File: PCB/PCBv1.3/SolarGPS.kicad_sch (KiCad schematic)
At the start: 54 parts, among them J1 Conn_01x24_Female, J2 Solar1+, J3 GND, J4 Conn_02x03_Odd_Even, J5 Solar2+, J6 GND, J7 Screw_Terminal_01x01, J8 Conn_01x04_Male, Q1 Q_NMOS_GSD, U1 STM32L011G4Ux, U2 MAX-M10Q, U6 LIS3DH, U7 TPS63802, Y1 32.768

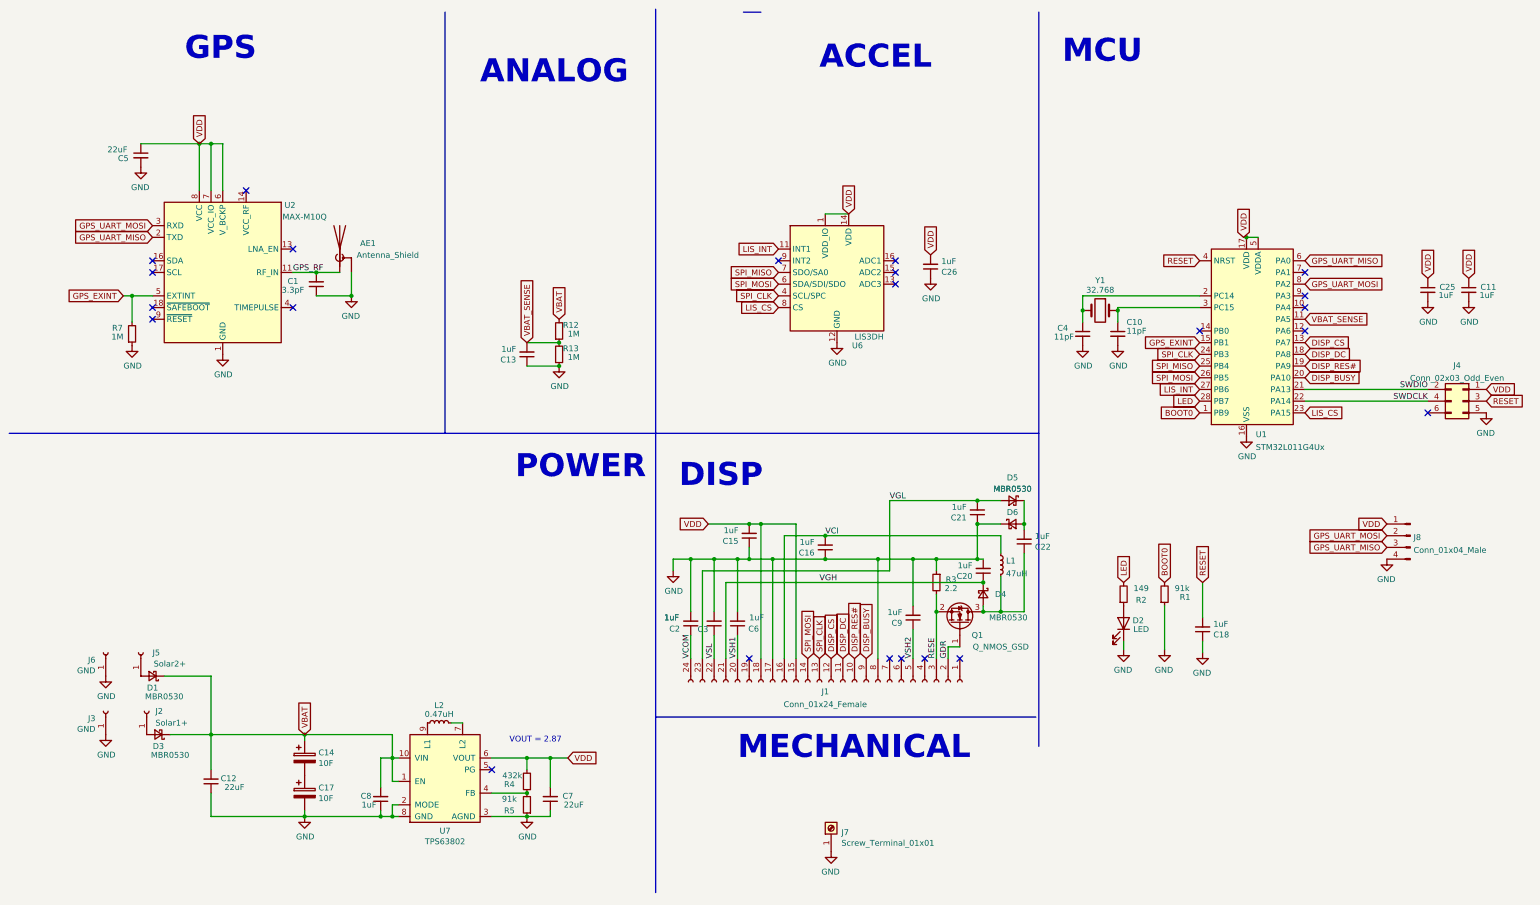
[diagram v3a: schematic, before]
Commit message: Rework power system for hybrid cap and bq25770
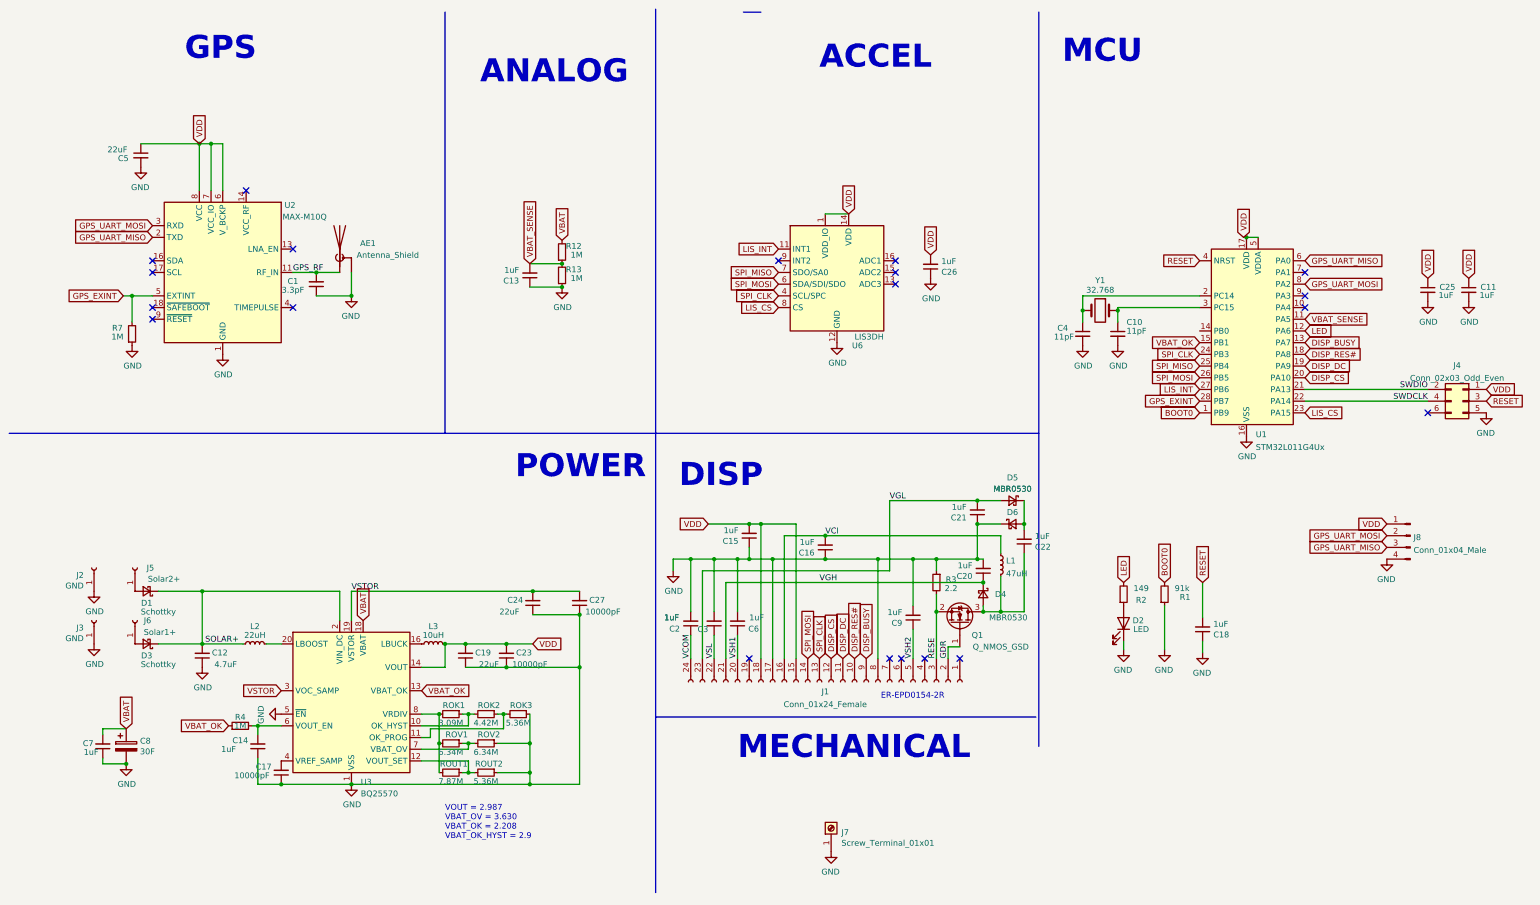
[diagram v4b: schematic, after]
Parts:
- removed C14, C17: 10F, Heliograph:SCCT20E106SRB_SMD, symbol Device:CP
- removed C8: 1uF, Capacitor_SMD:C_0603_1608Metric, symbol Device:C_Small
- removed R5: 91k, Resistor_SMD:R_0603_1608Metric, symbol Device:R_Small
- removed U7: TPS63802, Heliograph:VREG_TPS63802DLAR, symbol Heliograph:TPS63802-VeridianDesigns
- added C14: 1uF, Capacitor_SMD:C_0603_1608Metric, symbol Device:C_Small
- added C17, C23, C27: 10000pF, Capacitor_SMD:C_0603_1608Metric, symbol Device:C_Small
- added C19, C24: 22uF, Capacitor_SMD:C_0805_2012Metric, symbol Device:C_Small
- added C8: 30F, Heliograph:SCCT30E156SRB, symbol Device:CP
- added L3: 10uH, Heliograph:744029100, symbol Device:L_Small
- added ROK1: 3.09M, Resistor_SMD:R_0603_1608Metric, symbol Device:R_Small
- added ROK2: 4.42M, Resistor_SMD:R_0603_1608Metric, symbol Device:R_Small
- added ROK3, ROUT2: 5.36M, Resistor_SMD:R_0603_1608Metric, symbol Device:R_Small
- added ROUT1: 7.87M, Resistor_SMD:R_0603_1608Metric, symbol Device:R_Small
- added ROV1, ROV2: 6.34M, Resistor_SMD:R_0603_1608Metric, symbol Device:R_Small
- added U3: BQ25570, Package_DFN_QFN:QFN-20-1EP_3.5x3.5mm_P0.5mm_EP2x2mm, symbol Battery_Management:BQ25570
- C12: value 22uF -> 4.7uF; footprint Capacitor_SMD:C_0603_1608Metric -> Capacitor_SMD:C_0805_2012Metric; Part GRM187R61A226ME15 -> (none)
- C7: value 22uF -> 1uF; Part GRM187R61A226ME15 -> (none)
- D1, D3: value MBR0530 -> Schottky; footprint Diode_SMD:D_SOD-123 -> Diode_SMD:D_SOD-323_HandSoldering
- J2: value Solar1+ -> GND
- J6: value GND -> Solar1+
- L2: value 0.47uH -> 22uH; footprint Inductor_SMD:L_0806_2016Metric -> Heliograph:744031220; Part DFE201612E -> 744031220
- R4: value 432k -> 1M
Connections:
- net DISP_BUSY: now also U1.13 (PA7); no longer U1.20 (PA10)
- net DISP_CS: now also U1.20 (PA10); no longer U1.13 (PA7)
- net DISP_DC: now also U1.19 (PA9); no longer U1.18 (PA8)
- net DISP_RES#: now also U1.18 (PA8); no longer U1.19 (PA9)
- net GND: now also J2.1 (Pin_1), C14.1, C17.1, C19.1, C23.1, C24.1, C27.1, C8.2, ROK3.1, ROUT2.1, ROV2.1, U3.1 (VSS), U3.15 (VSS), U3.17 (VSS), U3.21 (VSS), U3.5 (~{EN}), U3.9 (VSS); no longer J6.1 (Pin_1)
- net GPS_EXINT: now also U1.28 (PB7); no longer U1.15 (PB1)
- net LED: now also U1.12 (PA6); no longer U1.28 (PB7)
- net VBAT: now also C7.2, C8.1, U3.18 (VBAT); no longer C12.2, D1.1 (K), D3.1 (K)
- net VDD: now also C19.2, C23.2, L3.2, U3.14 (VOUT); no longer C7.2, R4.2
- net VBAT_OK: now reaches R4.1
- net VBAT_OK: now also U1.15 (PB1), U3.13 (VBAT_OK)
- net at L2.2: now also U3.20 (LBOOST)
- net SOLAR+: now reaches L2.1
- net SOLAR+: now also C12.2, D1.1 (K), D3.1 (K), U3.2 (VIN_DC)
- net at D3.2 (A): now also J6.1 (Pin_1); no longer J2.1 (Pin_1)
- new net: ROK1.1, ROK2.2, U3.10 (OK_HYST)
- new net: ROK2.1, ROK3.2, U3.11 (OK_PROG)
- new net: ROUT1.1, ROUT2.2, U3.12 (VOUT_SET)
- new net: L3.1, U3.16 (LBUCK)
- new net: C17.2, U3.4 (VREF_SAMP)
- new net: C14.2, R4.2, U3.6 (VOUT_EN)
- new net: ROV1.1, ROV2.2, U3.7 (VBAT_OV)
- new net: ROK1.2, ROUT1.2, ROV1.2, U3.8 (VRDIV)
- new net VSTOR: C24.2, C27.2, U3.19 (VSTOR), U3.3 (VOC_SAMP)
- no-connect marks 23 -> 20
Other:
- note added: "ER-EPD0154-2R"
- note added: "VOUT = 2.987 VBAT_OV = 3.630 VBAT_OK = 2.208 VBAT_OK_HYST = 2.9"
- note removed: "VOUT = 2.87"
- moved on the sheet: C13, R12, R13

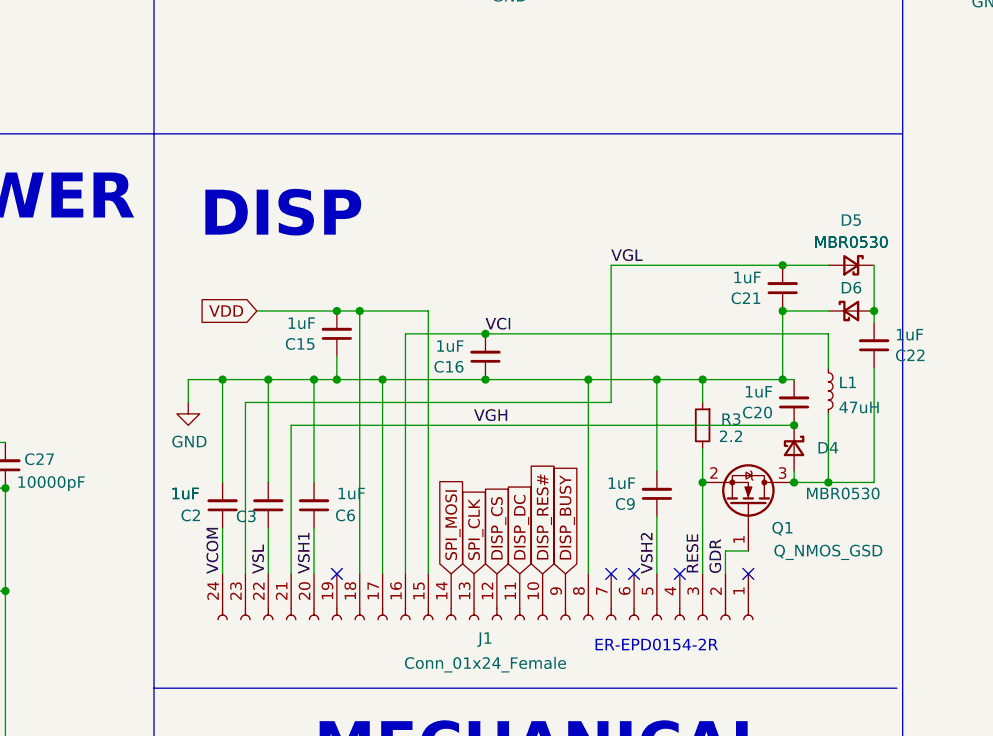
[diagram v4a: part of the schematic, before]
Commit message: Tweak Epaper driver
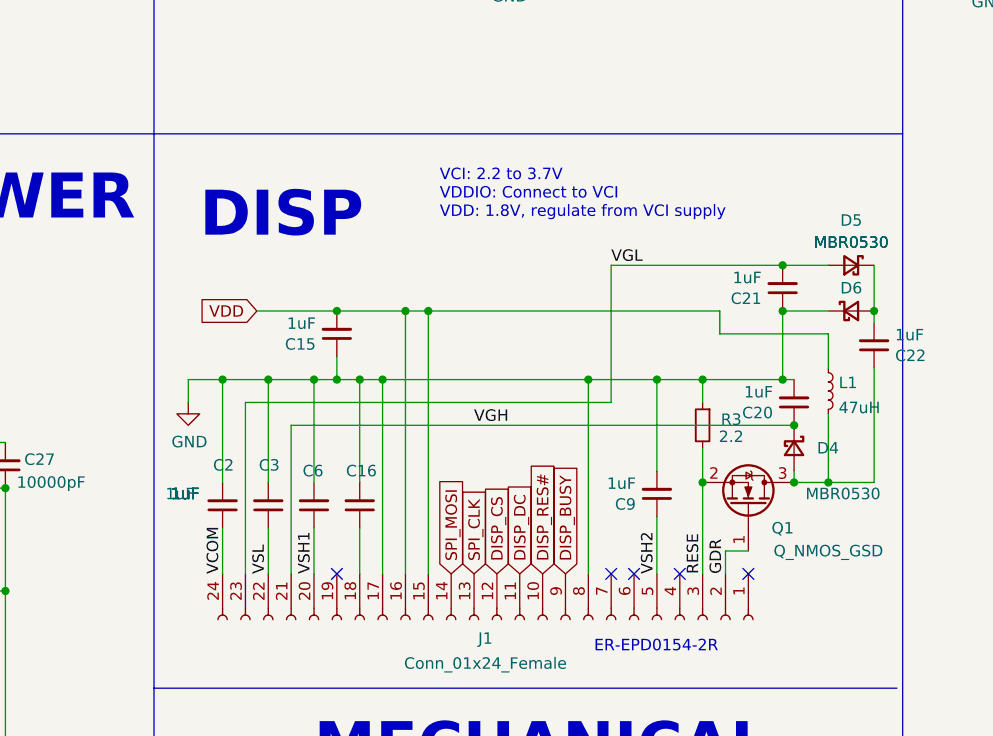
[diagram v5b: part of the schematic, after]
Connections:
- net GND: now also C16.2; no longer C16.1
- net VDD: now also J1.16 (Pin_16), L1.1; no longer J1.18 (Pin_18)
- removed net VCI: C16.2, J1.16 (Pin_16), L1.1
- new net: C16.1, J1.18 (Pin_18)
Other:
- note added: "VCI: 2.2 to 3.7V VDDIO: Connect to VCI VDD: 1.8V, regulate from VCI supply"
- moved on the sheet: C16
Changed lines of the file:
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@@
   (junction (at 111.125 149.225) (diameter 0) (color 0 0 0 0)
   )
-  (junction (at 189.23 130.81) (diameter 0) (color 0 0 0 0)
-  )
   (junction (at 232.41 123.19) (diameter 0) (color 0 0 0 0)
   )
@@
   (junction (at 66.04 167.005) (diameter 0) (color 0 0 0 0)
   )
+  (junction (at 182.88 123.19) (diameter 0) (color 0 0 0 0)
+  )
   (junction (at 135.89 142.875) (diameter 0) (color 0 0 0 0)
   )
@@
   (junction (at 125.095 177.165) (diameter 0) (color 0 0 0 0)
   )
+  (junction (at 180.34 123.19) (diameter 0) (color 0 0 0 0)
+  )
   (junction (at 245.11 76.835) (diameter 0) (color 0 0 0 0)
   )
+  (junction (at 175.26 130.81) (diameter 0) (color 0 0 0 0)
+  )
   (junction (at 222.25 118.11) (diameter 0) (color 0 0 0 0)
   )
@@
   (junction (at 208.28 130.81) (diameter 0) (color 0 0 0 0)
   )
-  (junction (at 189.23 125.73) (diameter 0) (color 0 0 0 0)
-  )
   (junction (at 132.08 66.675) (diameter 0) (color 0 0 0 0)
   )
@@
   )
   (junction (at 106.68 149.225) (diameter 0) (color 0 0 0 0)
-  )
-  (junction (at 175.26 123.19) (diameter 0) (color 0 0 0 0)
   )
   (junction (at 172.72 123.19) (diameter 0) (color 0 0 0 0)
@@
   (no_connect (at 43.18 66.04))
   (no_connect (at 73.66 76.2))
-  (wire (pts (xy 172.72 123.19) (xy 175.26 123.19))
+  (wire (pts (xy 172.72 123.19) (xy 180.34 123.19))
     (stroke (width 0) (type default) (color 0 0 0 0))
   )
@@
     (stroke (width 0) (type default) (color 0 0 0 0))
   )
+  (wire (pts (xy 215.265 123.19) (xy 215.265 125.73))
+    (stroke (width 0) (type default) (color 0 0 0 0))
+  )
   (wire (pts (xy 245.11 73.66) (xy 270.51 73.66))
     (stroke (width 0) (type default) (color 0 0 0 0))
@@
     (stroke (width 0) (type default) (color 0 0 0 0))
   )
-  (wire (pts (xy 175.26 123.19) (xy 182.88 123.19))
-    (stroke (width 0) (type default) (color 0 0 0 0))
-  )
   (wire (pts (xy 119.38 167.64) (xy 103.505 167.64))
     (stroke (width 0) (type default) (color 0 0 0 0))
@@
     (stroke (width 0) (type default) (color 0 0 0 0))
   )
+  (wire (pts (xy 180.34 123.19) (xy 182.88 123.19))
+    (stroke (width 0) (type default) (color 0 0 0 0))
+  )
   (wire (pts (xy 252.73 76.2) (xy 270.51 76.2))
     (stroke (width 0) (type default) (color 0 0 0 0))
@@
     (stroke (width 0) (type default) (color 0 0 0 0))
   )
-  (wire (pts (xy 189.23 125.73) (xy 180.34 125.73))
-    (stroke (width 0) (type default) (color 0 0 0 0))
-  )
   (wire (pts (xy 125.095 179.705) (xy 135.89 179.705))
     (stroke (width 0) (type default) (color 0 0 0 0))
@@
     (stroke (width 0) (type default) (color 0 0 0 0))
   )
+  (wire (pts (xy 175.26 130.81) (xy 177.8 130.81))
+    (stroke (width 0) (type default) (color 0 0 0 0))
+  )
   (wire (pts (xy 223.52 142.24) (xy 223.52 140.97))
     (stroke (width 0) (type default) (color 0 0 0 0))
@@
     (stroke (width 0) (type default) (color 0 0 0 0))
   )
+  (wire (pts (xy 182.88 123.19) (xy 215.265 123.19))
+    (stroke (width 0) (type default) (color 0 0 0 0))
+  )
   (wire (pts (xy 71.12 179.705) (xy 86.36 179.705))
     (stroke (width 0) (type default) (color 0 0 0 0))
   )
-  (wire (pts (xy 189.23 130.81) (xy 200.66 130.81))
+  (wire (pts (xy 177.8 130.81) (xy 200.66 130.81))
     (stroke (width 0) (type default) (color 0 0 0 0))
   )
@@
     (stroke (width 0) (type default) (color 0 0 0 0))
   )
-  (wire (pts (xy 180.34 125.73) (xy 180.34 152.4))
+  (wire (pts (xy 180.34 123.19) (xy 180.34 152.4))
     (stroke (width 0) (type default) (color 0 0 0 0))
   )
@@
     (stroke (width 0) (type default) (color 0 0 0 0))
   )
-  (wire (pts (xy 177.8 130.81) (xy 189.23 130.81))
-    (stroke (width 0) (type default) (color 0 0 0 0))
-  )
   (wire (pts (xy 125.095 66.675) (xy 132.08 66.675))
     (stroke (width 0) (type default) (color 0 0 0 0))
@@
     (stroke (width 0) (type default) (color 0 0 0 0))
   )
+  (wire (pts (xy 175.26 130.81) (xy 175.26 142.24))
+    (stroke (width 0) (type default) (color 0 0 0 0))
+  )
   (polyline (pts (xy 106.68 12.065) (xy 106.68 103.505))
     (stroke (width 0) (type default) (color 0 0 0 0))
@@
     (stroke (width 0) (type default) (color 0 0 0 0))
   )
-  (wire (pts (xy 172.72 130.81) (xy 177.8 130.81))
+  (wire (pts (xy 172.72 130.81) (xy 175.26 130.81))
     (stroke (width 0) (type default) (color 0 0 0 0))
   )
@@
     (stroke (width 0) (type default) (color 0 0 0 0))
   )
-  (wire (pts (xy 175.26 123.19) (xy 175.26 152.4))
-    (stroke (width 0) (type default) (color 0 0 0 0))
-  )
   (wire (pts (xy 125.095 71.755) (xy 132.08 71.755))
     (stroke (width 0) (type default) (color 0 0 0 0))
@@
     (stroke (width 0) (type default) (color 0 0 0 0))
   )
+  (wire (pts (xy 215.265 125.73) (xy 227.33 125.73))
+    (stroke (width 0) (type default) (color 0 0 0 0))
+  )
   (wire (pts (xy 119.38 164.465) (xy 119.38 167.64))
     (stroke (width 0) (type default) (color 0 0 0 0))
@@
     (stroke (width 0) (type default) (color 0 0 0 0))
   )
-  (wire (pts (xy 189.23 125.73) (xy 227.33 125.73))
+  (wire (pts (xy 175.26 147.32) (xy 175.26 152.4))
     (stroke (width 0) (type default) (color 0 0 0 0))
   )
@@
     (effects (font (size 5.0038 5.0038) (thickness 1.0008) bold) (justify left bottom))
   )
+  (text "VCI: 2.2 to 3.7V\nVDDIO: Connect to VCI\nVDD: 1.8V, regulate from VCI supply"
+    (at 184.15 113.03 0)
+    (effects (font (size 1.27 1.27)) (justify left bottom))
+  )
   (label "VSL" (at 165.1 152.4 90)
     (effects (font (size 1.27 1.27)) (justify left bottom))
@@
   )
   (label "VSTOR" (at 86.36 137.795 0)
-    (effects (font (size 1.27 1.27)) (justify left bottom))
-  )
-  (label "VCI" (at 189.23 125.73 0)
     (effects (font (size 1.27 1.27)) (justify left bottom))
   )
@@
   (symbol (lib_id "Device:C_Small") (at 165.1 144.78 180) (unit 1)
     (in_bom yes) (on_board yes)
-    (property "Reference" "C3" (id 0) (at 163.83 146.05 0)
+    (property "Reference" "C3" (id 0) (at 166.37 140.335 0)
       (effects (font (size 1.27 1.27)) (justify left))
     )
@@
   (symbol (lib_id "Device:C_Small") (at 160.02 144.78 180) (unit 1)
     (in_bom yes) (on_board yes)
-    (property "Reference" "C2" (id 0) (at 157.6832 145.9484 0)
+    (property "Reference" "C2" (id 0) (at 161.29 140.335 0)
       (effects (font (size 1.27 1.27)) (justify left))
     )
@@
   (symbol (lib_id "Device:C_Small") (at 170.18 144.78 0) (mirror x) (unit 1)
     (in_bom yes) (on_board yes)
-    (property "Reference" "C6" (id 0) (at 172.5168 145.9484 0)
-      (effects (font (size 1.27 1.27)) (justify left))
-    )
-    (property "Value" "1uF" (id 1) (at 172.72 143.51 0)
+    (property "Reference" "C6" (id 0) (at 168.91 140.97 0)
+      (effects (font (size 1.27 1.27)) (justify left))
+    )
+    (property "Value" "1uF" (id 1) (at 153.67 143.51 0)
       (effects (font (size 1.27 1.27)) (justify left))
     )
@@
     (pin "1")
   )
-  (symbol (lib_id "Device:C_Small") (at 189.23 128.27 180) (unit 1)
-    (in_bom yes) (on_board yes)
-    (property "Reference" "C16" (id 0) (at 186.8932 129.4384 0)
-      (effects (font (size 1.27 1.27)) (justify left))
-    )
-    (property "Value" "1uF" (id 1) (at 186.8932 127.127 0)
-      (effects (font (size 1.27 1.27)) (justify left))
-    )
-    (property "Footprint" "Capacitor_SMD:C_0603_1608Metric" (id 2) (at 189.23 128.27 0)
-      (effects (font (size 1.27 1.27)) hide)
-    )
-    (property "Datasheet" "~" (id 3) (at 189.23 128.27 0)
-      (effects (font (size 1.27 1.27)) hide)
-    )
+  (symbol (lib_id "Device:C_Small") (at 175.26 144.78 180) (unit 1)
+    (in_bom yes) (on_board yes)
+    (property "Reference" "C16" (id 0) (at 177.165 140.97 0)
+      (effects (font (size 1.27 1.27)) (justify left))
+    )
+    (property "Value" "1uF" (id 1) (at 157.48 143.51 0)
+      (effects (font (size 1.27 1.27)) (justify left))
+    )
+    (property "Footprint" "Capacitor_SMD:C_0603_1608Metric" (id 2) (at 175.26 144.78 0)
+      (effects (font (size 1.27 1.27)) hide)
+    )
+    (property "Datasheet" "~" (id 3) (at 175.26 144.78 0)
+      (effects (font (size 1.27 1.27)) hide)
+    )
